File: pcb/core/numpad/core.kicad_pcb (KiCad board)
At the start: 2 copper layers, 79.3 x 94.5 mm, 28 parts, among them J1 Conn_01x11, J2 Conn_01x11, SW1 SW_Push_45deg, SW10 SW_Push_45deg, SW2 SW_Push_45deg, SW3 SW_Push_45deg, SW4 SW_Push_45deg, SW5 SW_Push_45deg, SW6 SW_Push_45deg, SW7 SW_Push_45deg, SW8 SW_Push_45deg, SW9 SW_Push_45deg, U1 Helios

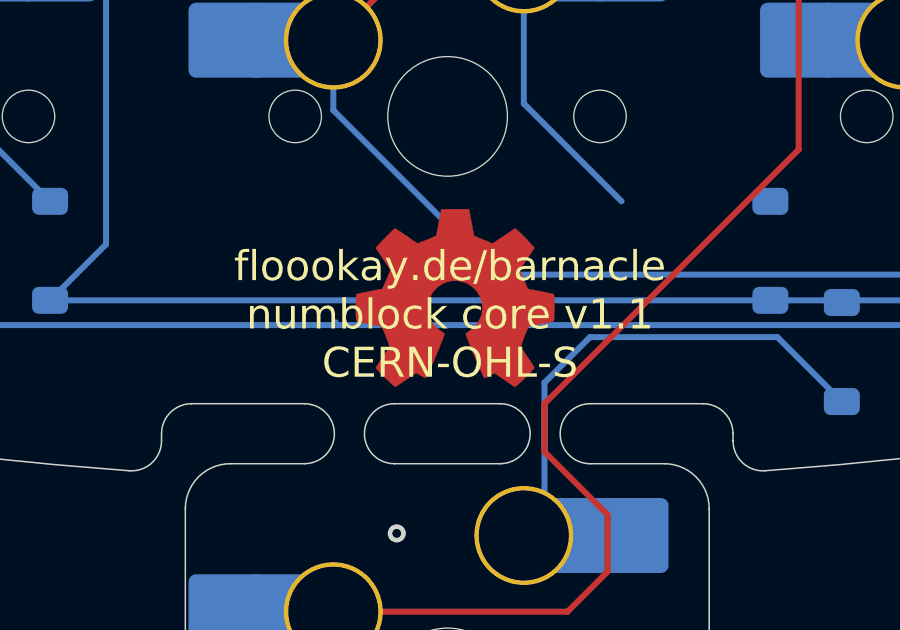
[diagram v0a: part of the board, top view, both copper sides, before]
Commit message: fixed name on pcb
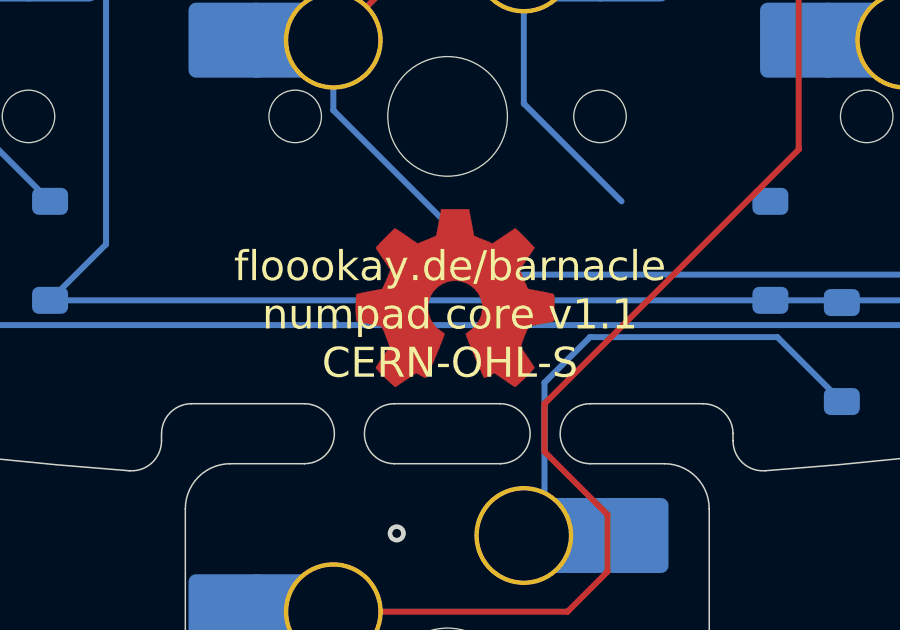
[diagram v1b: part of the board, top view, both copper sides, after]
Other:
- board text added: "floookay.de/barnacle numpad core v1.1 CERN-OHL-S"
- board text removed: "floookay.de/barnacle numblock core v1.1 CERN-OHL-S"
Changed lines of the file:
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@@
 		(layer "User.2")
 	)
-	(gr_text "floookay.de/barnacle\nnumblock core v1.1\nCERN-OHL-S"
+	(gr_text "floookay.de/barnacle\nnumpad core v1.1\nCERN-OHL-S"
 		(at 198.275 209.9 0)
 		(layer "F.SilkS")
